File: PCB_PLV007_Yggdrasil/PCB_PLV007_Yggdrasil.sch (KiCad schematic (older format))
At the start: 44 parts, among them J1 Conn_01x12, U7 BME280, U8 SN65HVD232

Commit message: Odin routing
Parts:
- removed C13, C15, C22, C23: 10uF, symbol Device:C
- removed C16, C8: 0.1uF, symbol Device:C
- removed C17: 1uF, symbol Device:C
- removed R18: 4.7K, symbol Device:R_US
- removed R21, R22: 0, symbol Device:R_US
- added C? (x4): 10uF, Capacitor_SMD:C_1210_3225Metric_Pad1.42x2.65mm_HandSolder, symbol Device:C
- added C?: 1uF, Capacitor_SMD:C_0603_1608Metric_Pad1.05x0.95mm_HandSolder, symbol Device:C
- added C? (x2): 0.1uF, Capacitor_SMD:C_0603_1608Metric_Pad1.05x0.95mm_HandSolder, symbol Device:C
- added R?: 4.7K, Resistor_SMD:R_0603_1608Metric_Pad1.05x0.95mm_HandSolder, symbol Device:R_US
- added R? (x2): 0, Resistor_SMD:R_0603_1608Metric_Pad1.05x0.95mm_HandSolder, symbol Device:R_US
- C10: footprint (none) -> Capacitor_SMD:C_0603_1608Metric_Pad1.05x0.95mm_HandSolder; MFPN (none) -> CL10B105KA8NNNC
- C11, C12, R45: footprint (none) -> Capacitor_SMD:C_0603_1608Metric_Pad1.05x0.95mm_HandSolder
- C14: footprint (none) -> Capacitor_SMD:C_0603_1608Metric_Pad1.05x0.95mm_HandSolder; MFPN (none) -> CC0603KRX7R8BB104
- C9: footprint (none) -> Capacitor_SMD:C_1210_3225Metric_Pad1.42x2.65mm_HandSolder; MFPN (none) -> GRM32EC72A106KE05L
- C?: footprint (none) -> Capacitor_THT:CP_Radial_D6.3mm_P2.50mm; MFPN (none) -> UVR1H470MED
- D1: footprint (none) -> BoringFootprints:DO-221AC; MFPN (none) -> VSSAF5N50-M3/6A
- F1: footprint (none) -> BoringFootprints:BelFuse_0679H; MFPN (none) -> 0679H2000-05
- J1: footprint (none) -> Connector_Molex:Molex_Micro-Fit_3.0_43045-1200_2x06_P3.00mm_Horizontal; MFPN (none) -> 0430451200
- JP1: footprint (none) -> Jumper:SolderJumper-2_P1.3mm_Open_RoundedPad1.0x1.5mm
- JP2: footprint (none) -> Jumper:SolderJumper-3_P1.3mm_Open_RoundedPad1.0x1.5mm_NumberLabels
- R13: footprint (none) -> Resistor_SMD:R_0603_1608Metric_Pad1.05x0.95mm_HandSolder; MFPN (none) -> RMCF0603FT4K70
- R20, R40, R41, R43, R44: footprint (none) -> Resistor_SMD:R_0603_1608Metric_Pad1.05x0.95mm_HandSolder
- R26: footprint (none) -> Resistor_SMD:R_1210_3225Metric_Pad1.42x2.65mm_HandSolder; MFPN (none) -> RMCF1210FT120R
- R39, R42: value DNP -> 0; footprint (none) -> Resistor_SMD:R_0603_1608Metric_Pad1.05x0.95mm_HandSolder
- U8: MFPN (none) -> SN65HVD232DR
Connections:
- net +12V: now also C?.1, C?.1, C?.1, C?.1
- net +3V3: now also C?.1, C?.1, C?.1, R?.1
- net +5V: now also R?.2, R?.2
- net AvionicsHeartbeatTemplate/HEARTBEAT_INPUT_6: now also R?.1
- net AvionicsHeartbeatTemplate/HEARTBEAT_INPUT_7: now also R?.1
- net GND: now also C?.2, C?.2, C?.2, C?.2, C?.2, C?.2, C?.2
- net I2C_SDA: now also R?.2

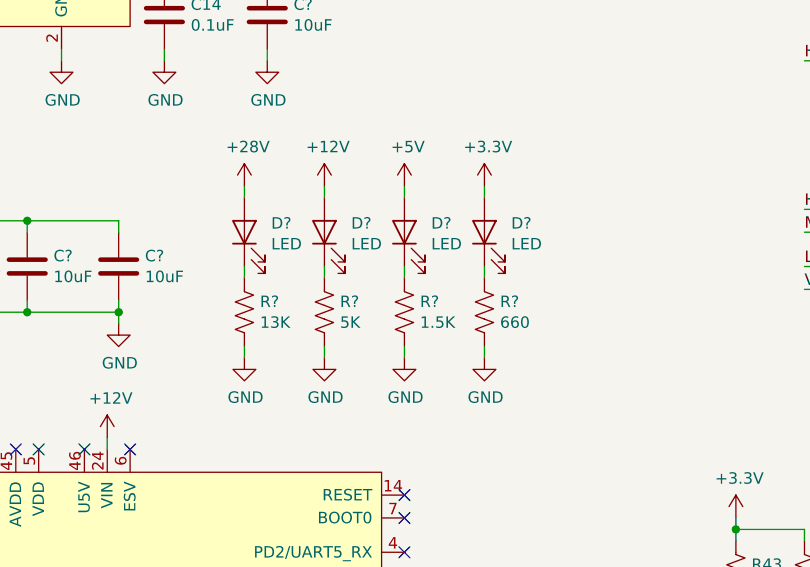
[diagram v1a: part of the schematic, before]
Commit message: Fix transistors in heartbeat circuits
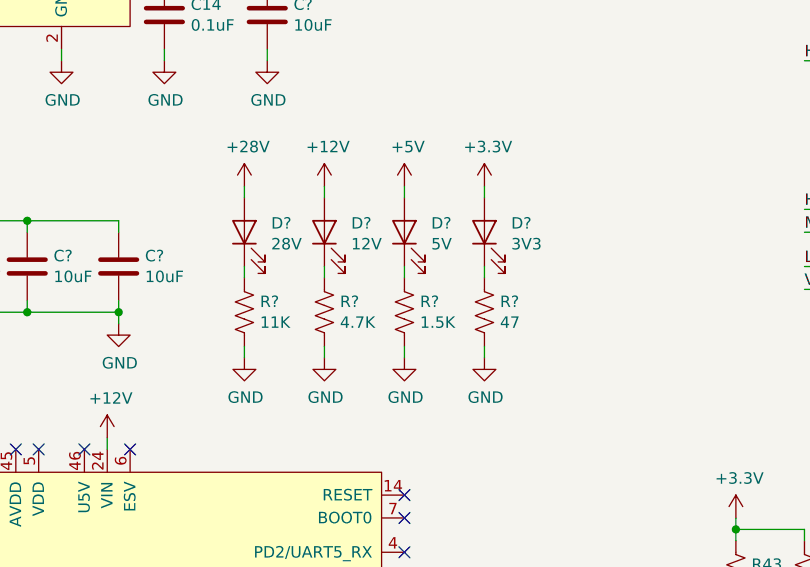
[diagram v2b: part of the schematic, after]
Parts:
- removed D? (x3): LED, symbol Device:LED
- added D?: 12V, LED_SMD:LED_0805_2012Metric_Pad1.15x1.40mm_HandSolder, symbol Device:LED
- added D?: 5V, LED_SMD:LED_0805_2012Metric_Pad1.15x1.40mm_HandSolder, symbol Device:LED
- added D?: 3V3, LED_SMD:LED_0805_2012Metric_Pad1.15x1.40mm_HandSolder, symbol Device:LED
- D?: value LED -> 28V; footprint (none) -> LED_SMD:LED_0805_2012Metric_Pad1.15x1.40mm_HandSolder; MFPN (none) -> 150080GS75000
- R?: value 13K -> 11K; footprint (none) -> Resistor_SMD:R_0603_1608Metric_Pad1.05x0.95mm_HandSolder; MFPN (none) -> RMCF0603FT11K0
- R?: value 5K -> 4.7K; footprint (none) -> Resistor_SMD:R_0603_1608Metric_Pad1.05x0.95mm_HandSolder; MFPN (none) -> RMCF0603FT4K70
- R?: footprint (none) -> Resistor_SMD:R_0603_1608Metric_Pad1.05x0.95mm_HandSolder; MFPN (none) -> RMCF0603FT1K50
- R?: value 660 -> 47; footprint (none) -> Resistor_SMD:R_0603_1608Metric_Pad1.05x0.95mm_HandSolder; MFPN (none) -> RMCF0603FT50R0
- U7: MFPN (none) -> BME280
- VR1: MFPN (none) -> R-78C12-1.0
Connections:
- net +12V: now also D?.2 (A)
- net +3V3: now also D?.2 (A)
- net +5V: now also D?.2 (A)
- net at R?.1: now also D?.1 (K) (x3)
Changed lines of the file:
@@
 F 2 "Package_LGA:Bosch_LGA-8_2.5x2.5mm_P0.65mm_ClockwisePinNumbering" H 7400 5450 50  0001 C CNN
 F 3 "https://www.bosch-sensortec.com/media/boschsensortec/downloads/datasheets/bst-bme280-ds002.pdf" H 7400 5450 50  0001 C CNN
-F 4 "" H 7400 5650 50  0001 C CNN "MFPN"
+F 4 "BME280" H 7400 5650 50  0001 C CNN "MFPN"
 	1    7400 5650
 	1    0    0    -1
@@
 F 2 "BoringFootprints:Recom_R-78c-1.0" H 3750 850 50  0001 C CNN
 F 3 "https://recom-power.com/pdf/Innoline/R-78C-1.0.pdf" H 3750 850 50  0001 C CNN
+F 4 "R-78C12-1.0" H 3550 1150 50  0001 C CNN "MFPN"
 	1    3550 1150
 	1    0    0    -1
@@
 P 4350 2300
 F 0 "D?" V 4389 2183 50  0000 R CNN
-F 1 "LED" V 4298 2183 50  0000 R CNN
-F 2 "" H 4350 2300 50  0001 C CNN
-F 3 "~" H 4350 2300 50  0001 C CNN
+F 1 "28V" V 4298 2183 50  0000 R CNN
+F 2 "LED_SMD:LED_0805_2012Metric_Pad1.15x1.40mm_HandSolder" H 4350 2300 50  0001 C CNN
+F 3 "https://www.we-online.de/katalog/datasheet/150080GS75000.pdf" H 4350 2300 50  0001 C CNN
+F 4 "150080GS75000" V 4350 2300 50  0001 C CNN "MFPN"
 	1    4350 2300
 	0    -1   -1   0
@@
 P 4350 2650
 F 0 "R?" H 4418 2696 50  0000 L CNN
-F 1 "13K" H 4418 2605 50  0000 L CNN
-F 2 "" V 4390 2640 50  0001 C CNN
-F 3 "~" H 4350 2650 50  0001 C CNN
+F 1 "11K" H 4418 2605 50  0000 L CNN
+F 2 "Resistor_SMD:R_0603_1608Metric_Pad1.05x0.95mm_HandSolder" V 4390 2640 50  0001 C CNN
+F 3 "https://www.seielect.com/catalog/sei-rmcf_rmcp.pdf" H 4350 2650 50  0001 C CNN
+F 4 "RMCF0603FT11K0" H 4350 2650 50  0001 C CNN "MFPN"
 	1    4350 2650
 	1    0    0    -1
@@
 	1    0    0    -1
 $EndComp
-$Comp
-L Device:LED D?
-U 1 1 5FD4DFAC
-P 4700 2300
-F 0 "D?" V 4739 2183 50  0000 R CNN
-F 1 "LED" V 4648 2183 50  0000 R CNN
-F 2 "" H 4700 2300 50  0001 C CNN
-F 3 "~" H 4700 2300 50  0001 C CNN
-	1    4700 2300
-	0    -1   -1   0
-$EndComp
 Wire Wire Line
 	4700 2100 4700 2150
@@
 P 4700 2650
 F 0 "R?" H 4768 2696 50  0000 L CNN
-F 1 "5K" H 4768 2605 50  0000 L CNN
-F 2 "" V 4740 2640 50  0001 C CNN
-F 3 "~" H 4700 2650 50  0001 C CNN
+F 1 "4.7K" H 4768 2605 50  0000 L CNN
+F 2 "Resistor_SMD:R_0603_1608Metric_Pad1.05x0.95mm_HandSolder" V 4740 2640 50  0001 C CNN
+F 3 "https://www.seielect.com/catalog/sei-rmcf_rmcp.pdf" H 4700 2650 50  0001 C CNN
+F 4 "RMCF0603FT4K70" H 4700 2650 50  0001 C CNN "MFPN"
 	1    4700 2650
 	1    0    0    -1
@@
 	1    0    0    -1
 $EndComp
-$Comp
-L Device:LED D?
-U 1 1 5FD58925
-P 5050 2300
-F 0 "D?" V 5089 2183 50  0000 R CNN
-F 1 "LED" V 4998 2183 50  0000 R CNN
-F 2 "" H 5050 2300 50  0001 C CNN
-F 3 "~" H 5050 2300 50  0001 C CNN
-	1    5050 2300
-	0    -1   -1   0
-$EndComp
 Wire Wire Line
 	5050 2100 5050 2150
@@
 F 0 "R?" H 5118 2696 50  0000 L CNN
 F 1 "1.5K" H 5118 2605 50  0000 L CNN
-F 2 "" V 5090 2640 50  0001 C CNN
-F 3 "~" H 5050 2650 50  0001 C CNN
+F 2 "Resistor_SMD:R_0603_1608Metric_Pad1.05x0.95mm_HandSolder" V 5090 2640 50  0001 C CNN
+F 3 "https://www.seielect.com/catalog/sei-rmcf_rmcp.pdf" H 5050 2650 50  0001 C CNN
+F 4 "RMCF0603FT1K50" H 5050 2650 50  0001 C CNN "MFPN"
 	1    5050 2650
 	1    0    0    -1
@@
 	1    0    0    -1
 $EndComp
-$Comp
-L Device:LED D?
-U 1 1 5FD58950
-P 5400 2300
-F 0 "D?" V 5439 2183 50  0000 R CNN
-F 1 "LED" V 5348 2183 50  0000 R CNN
-F 2 "" H 5400 2300 50  0001 C CNN
-F 3 "~" H 5400 2300 50  0001 C CNN
-	1    5400 2300
-	0    -1   -1   0
-$EndComp
 Wire Wire Line
 	5400 2100 5400 2150
@@
 P 5400 2650
 F 0 "R?" H 5468 2696 50  0000 L CNN
-F 1 "660" H 5468 2605 50  0000 L CNN
-F 2 "" V 5440 2640 50  0001 C CNN
-F 3 "~" H 5400 2650 50  0001 C CNN
+F 1 "47" H 5468 2605 50  0000 L CNN
+F 2 "Resistor_SMD:R_0603_1608Metric_Pad1.05x0.95mm_HandSolder" V 5440 2640 50  0001 C CNN
+F 3 "https://www.seielect.com/catalog/sei-rmcf_rmcp.pdf" H 5400 2650 50  0001 C CNN
+F 4 "RMCF0603FT50R0" H 5400 2650 50  0001 C CNN "MFPN"
 	1    5400 2650
 	1    0    0    -1
@@
 	0    1    1    0
 $EndComp
+$Comp
+L Device:LED D?
+U 1 1 5FEC1BD0
+P 4700 2300
+F 0 "D?" V 4739 2183 50  0000 R CNN
+F 1 "12V" V 4648 2183 50  0000 R CNN
+F 2 "LED_SMD:LED_0805_2012Metric_Pad1.15x1.40mm_HandSolder" H 4700 2300 50  0001 C CNN
+F 3 "https://www.we-online.de/katalog/datasheet/150080GS75000.pdf" H 4700 2300 50  0001 C CNN
+F 4 "150080GS75000" V 4700 2300 50  0001 C CNN "MFPN"
+	1    4700 2300
+	0    -1   -1   0
+$EndComp
+$Comp
+L Device:LED D?
+U 1 1 5FEC205D
+P 5050 2300
+F 0 "D?" V 5089 2183 50  0000 R CNN
+F 1 "5V" V 4998 2183 50  0000 R CNN
+F 2 "LED_SMD:LED_0805_2012Metric_Pad1.15x1.40mm_HandSolder" H 5050 2300 50  0001 C CNN
+F 3 "https://www.we-online.de/katalog/datasheet/150080GS75000.pdf" H 5050 2300 50  0001 C CNN
+F 4 "150080GS75000" V 5050 2300 50  0001 C CNN "MFPN"
+	1    5050 2300
+	0    -1   -1   0
+$EndComp
+$Comp
+L Device:LED D?
+U 1 1 5FEC2466
+P 5400 2300
+F 0 "D?" V 5439 2183 50  0000 R CNN
+F 1 "3V3" V 5348 2183 50  0000 R CNN
+F 2 "LED_SMD:LED_0805_2012Metric_Pad1.15x1.40mm_HandSolder" H 5400 2300 50  0001 C CNN
+F 3 "https://www.we-online.de/katalog/datasheet/150080GS75000.pdf" H 5400 2300 50  0001 C CNN
+F 4 "150080GS75000" V 5400 2300 50  0001 C CNN "MFPN"
+	1    5400 2300
+	0    -1   -1   0
+$EndComp
 $EndSCHEMATC

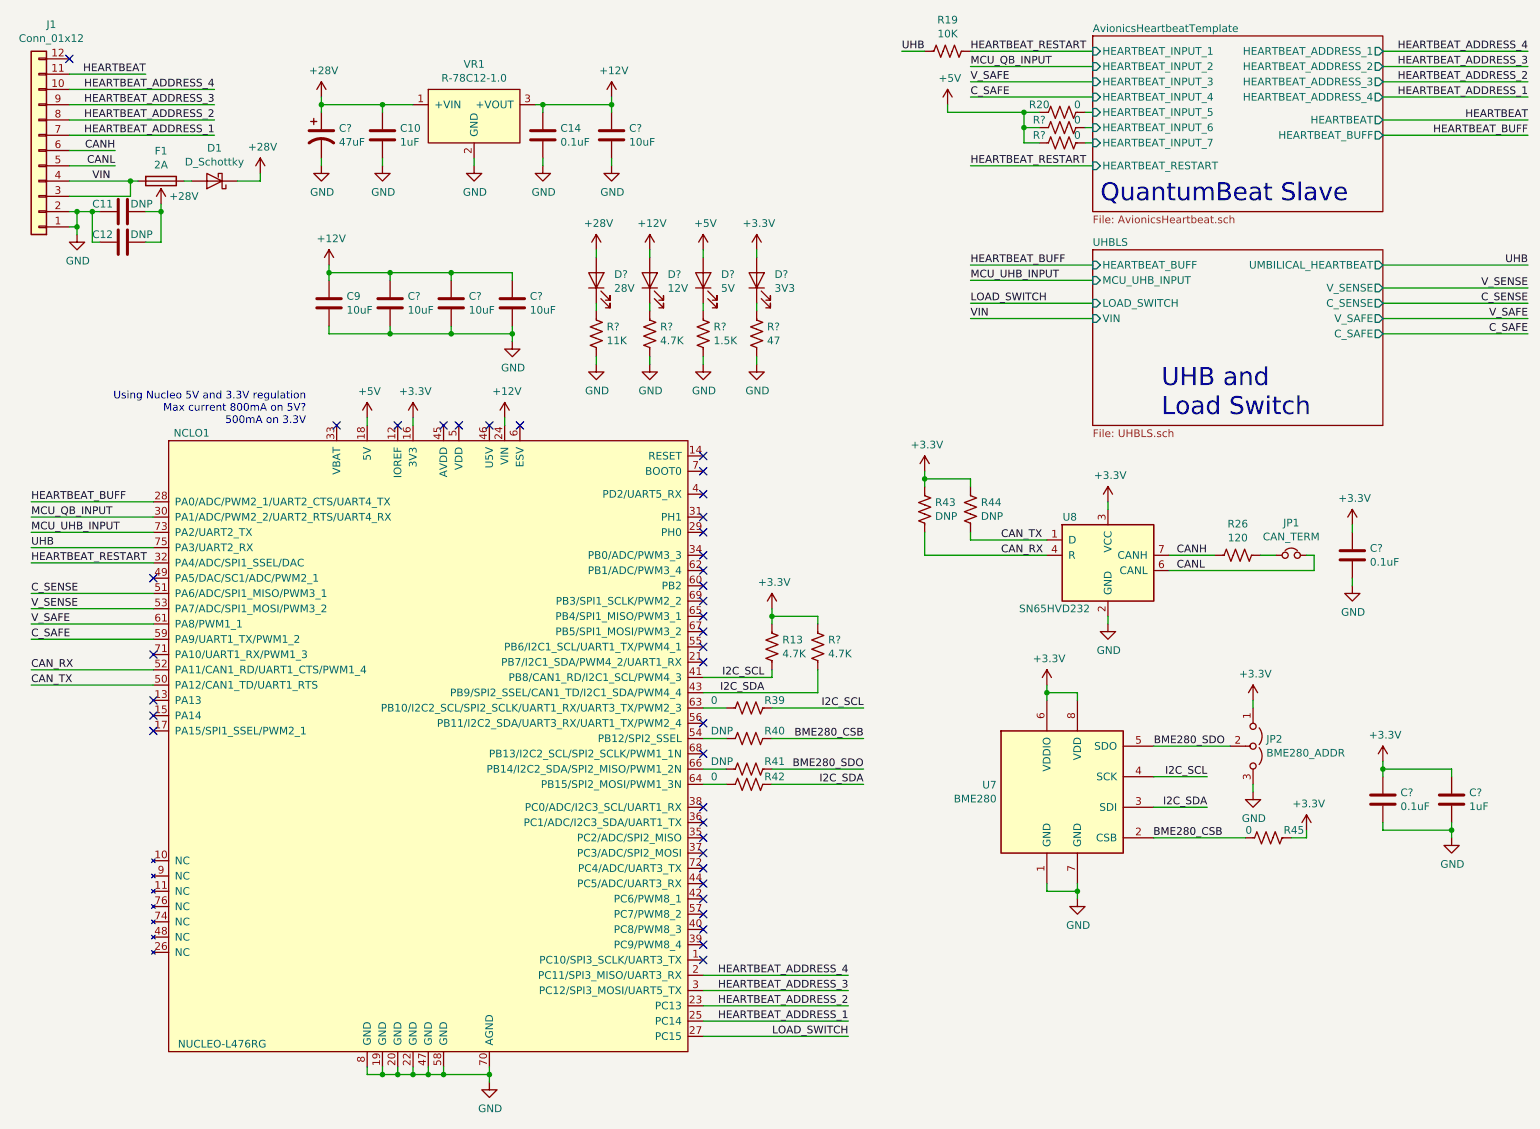
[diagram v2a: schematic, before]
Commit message: Odin Silk, finish Yggdrasil component selection
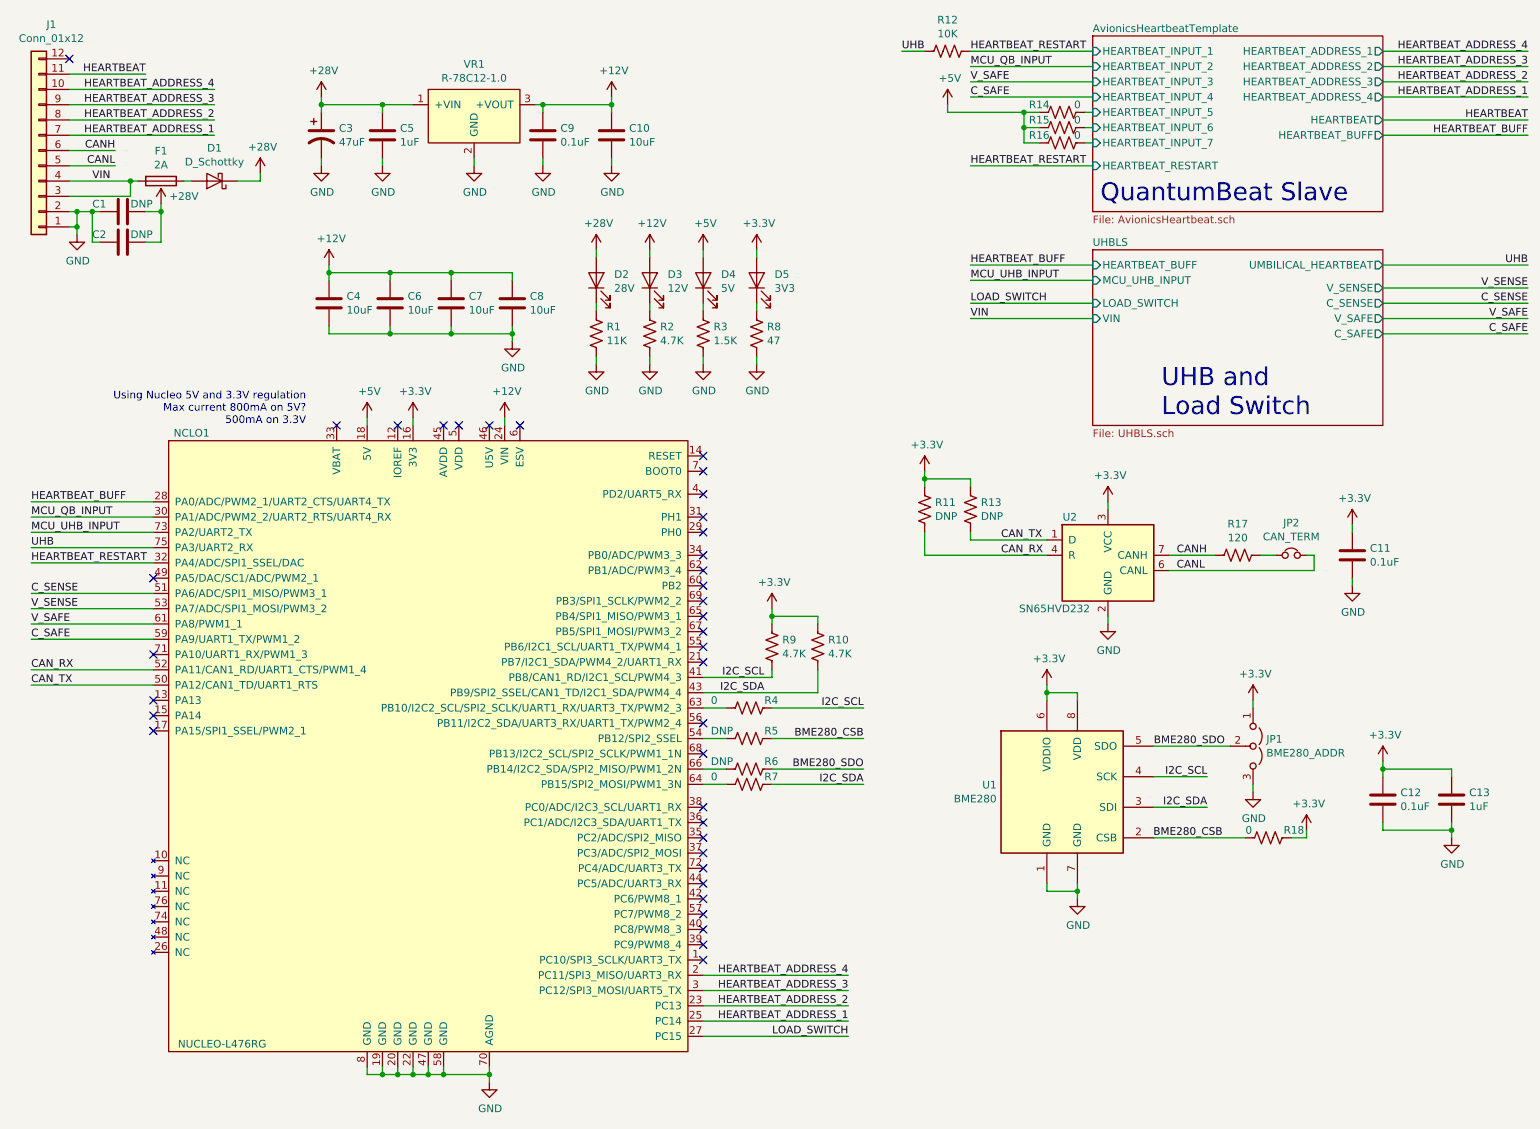
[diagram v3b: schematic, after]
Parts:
- R12: renamed from R19; footprint (none) -> Resistor_SMD:R_0603_1608Metric_Pad1.05x0.95mm_HandSolder; MFPN (none) -> RMCF0603FT10K0
- gave numbers to parts that had none: 19
- renumbered C11 to C1, C12 to C2, C9 to C4, C10 to C5, C14 to C9, JP2 to JP1, JP1 to JP2, R43 to R11, R44 to R13, R20 to R14, R26 to R17, R45 to R18, R39 to R4, R40 to R5, R41 to R6, R42 to R7, R13 to R9, U7 to U1, U8 to U2
